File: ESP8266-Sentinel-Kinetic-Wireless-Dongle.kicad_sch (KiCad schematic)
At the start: 55 parts, among them J1 Conn_01x04, J2 Screw_Terminal_01x04, J3 Conn_01x06_Pin, J4 RJ9, J5 Screw_Terminal_01x03, J6 Screw_Terminal_01x02, Q1 AO3400A, SW2 SW_Push, SW4 SW_Push, U1 AMS1117-3.3, U2 ESP-12F, U3 MAX3232, U4 ESP32-WROOM-32, U5 L78L12_SOT89, U6 PC817

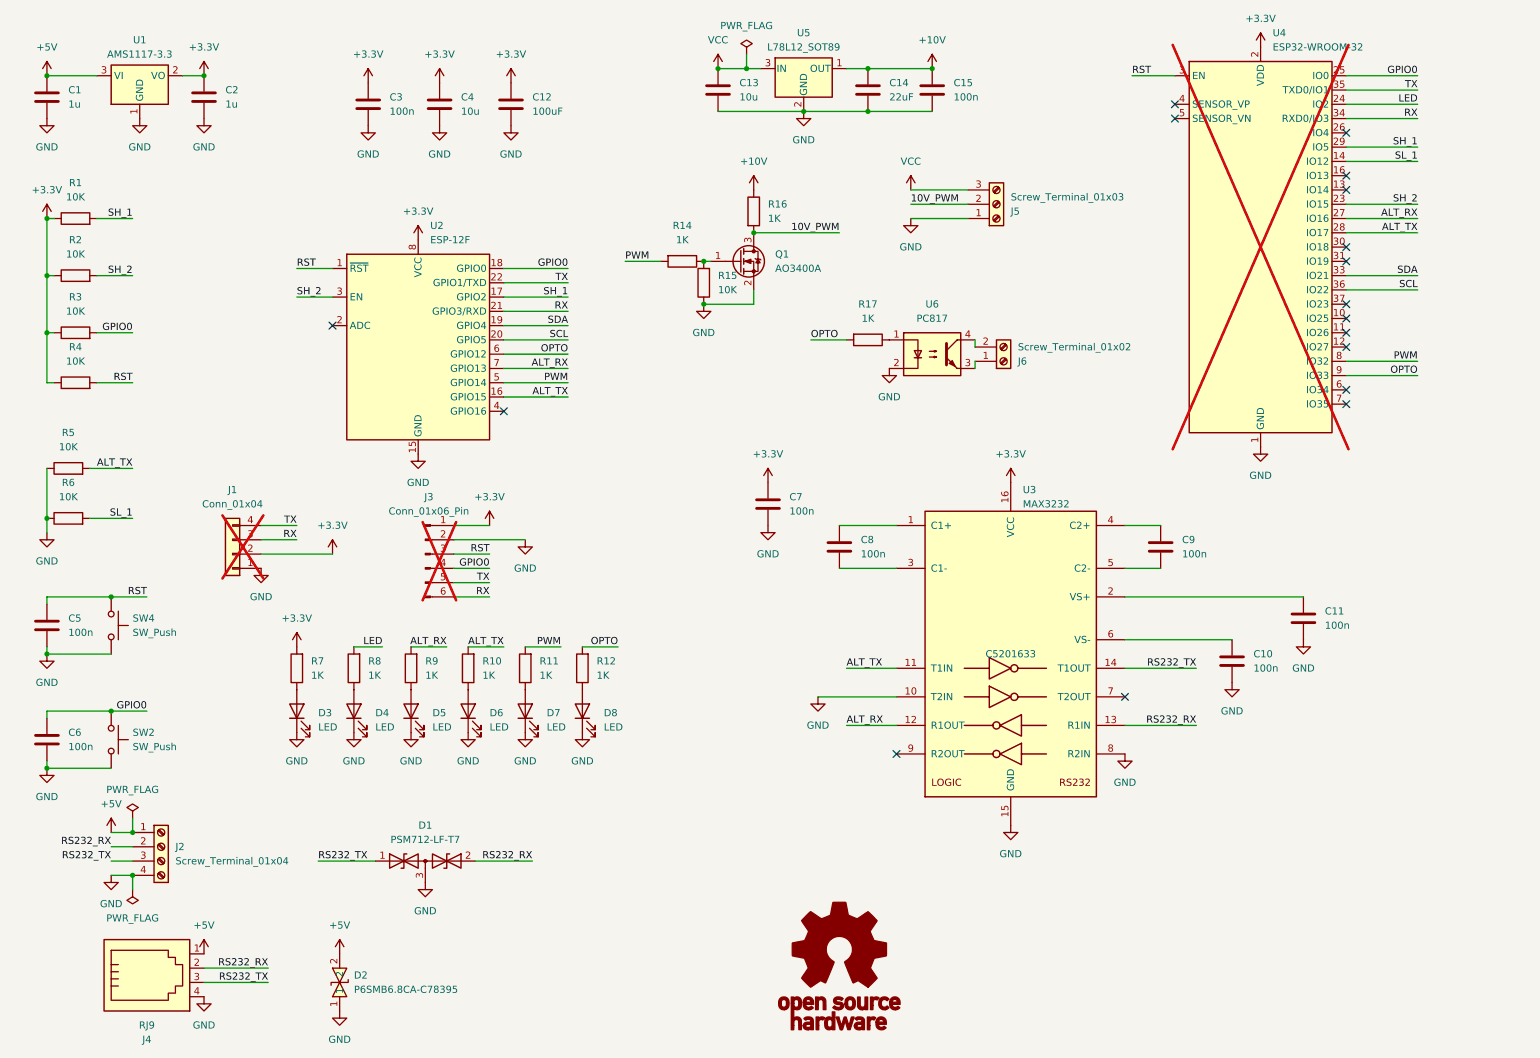
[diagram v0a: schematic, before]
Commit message: Completed PCB Layout Added PWM Rail to rail Added Silkscreen markings
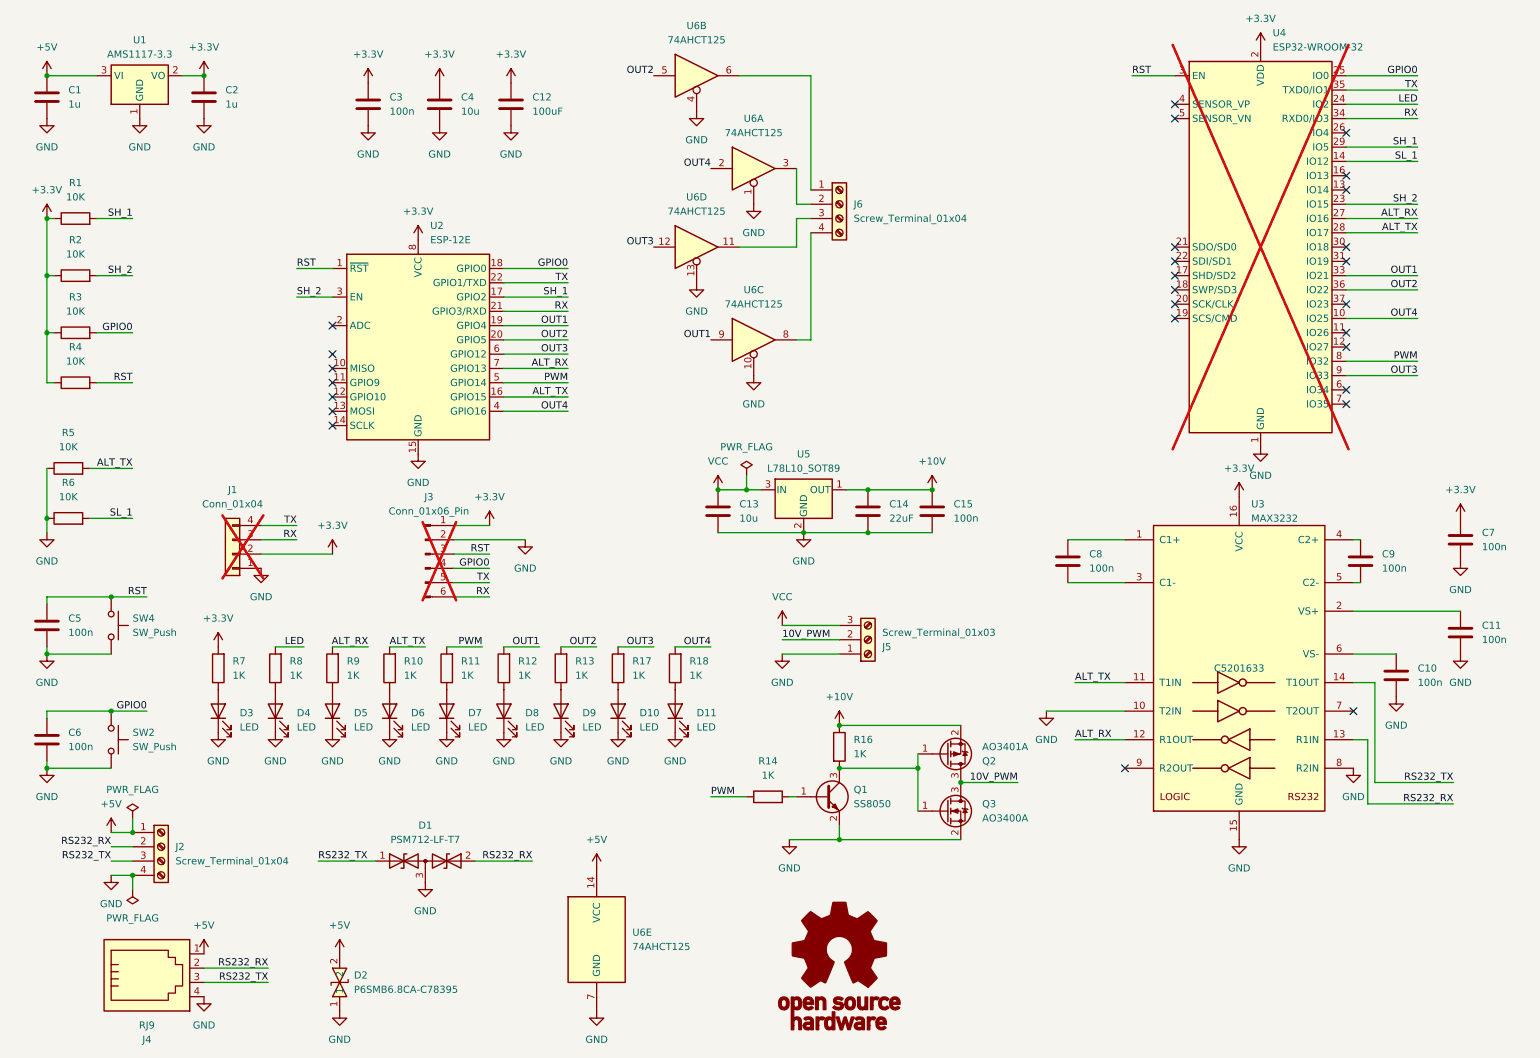
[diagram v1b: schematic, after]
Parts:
- removed J6: Screw_Terminal_01x02, TerminalBlock_4Ucon:TerminalBlock_4Ucon_1x02_P3.50mm_Horizontal, symbol Connector:Screw_Terminal_01x02
- removed Q1: AO3400A, Package_TO_SOT_SMD:SOT-23, symbol Transistor_FET:AO3400A
- removed R15: 10K, Resistor_SMD:R_0402_1005Metric, symbol Device:R
- removed U5: L78L12_SOT89, Package_TO_SOT_SMD:SOT-89-3, symbol Regulator_Linear:L78L12_SOT89
- removed U6: PC817, Package_DIP:DIP-4_W7.62mm, symbol Isolator:PC817
- added D10, D11, D9: LED, LED_SMD:LED_0603_1608Metric, symbol Device:LED
- added J6: Screw_Terminal_01x04, TerminalBlock_4Ucon:TerminalBlock_4Ucon_1x04_P3.50mm_Horizontal, symbol Connector:Screw_Terminal_01x04
- added Q1: SS8050, Package_TO_SOT_SMD:SOT-23, symbol Transistor_BJT:SS8050
- added Q2: AO3401A, Package_TO_SOT_SMD:SOT-23, symbol Transistor_FET:AO3401A
- added Q3: AO3400A, Package_TO_SOT_SMD:SOT-23, symbol Transistor_FET:AO3400A
- added R13, R18: 1K, Resistor_SMD:R_0402_1005Metric, symbol Device:R
- added U5: L78L10_SOT89, Package_TO_SOT_SMD:SOT-89-3, symbol Regulator_Linear:L78L10_SOT89
- added U6: 74AHCT125, Package_DIP:DIP-14_W7.62mm, symbol 74xx:74AHCT125
- U2: value ESP-12F -> ESP-12E
- U4: symbol lib:ESP32-WROOM-32 -> RF_Module:ESP32-WROOM-32
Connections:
- net +10V: now also Q2.2 (S), U5.1 (OUT)
- net +5V: now also U6.14 (VCC)
- net 10V_PWM: now also Q2.3 (D), Q3.3 (D); no longer R16.2
- net GND: now also D10.1 (K), D11.1 (K), D9.1 (K), Q1.2 (E), Q3.2 (S), U5.2 (GND), U6.1, U6.10, U6.13, U6.4, U6.7 (GND)
- net PWM: now also R14.1; no longer R14.2
- net VCC: now also U5.3 (IN)
- net at R17.1: now also D10.2 (A)
- net OUT4: now reaches U4.10 (IO25)
- net OUT4: now also U2.4 (GPIO16), R18.2, U6.2
- net OPTO renamed OUT3
- net OUT3: now also U6.12; no longer R12.2
- net SCL renamed OUT2
- net OUT2: now also R13.2, U6.5
- net SDA renamed OUT1
- net OUT1: now also R12.2, U6.9
- new net: Q1.1 (B), R14.2
- new net: Q1.3 (C), Q2.1 (G), Q3.1 (G), R16.2
- new net: J6.4 (Pin_4), U6.8
- new net: J6.3 (Pin_3), U6.11
- new net: J6.2 (Pin_2), U6.3
- new net: J6.1 (Pin_1), U6.6
- new net: D11.2 (A), R18.1
- new net: D9.2 (A), R13.1
- no-connect marks 17 -> 27
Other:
- moved on the sheet: C10, C11, C13, C14, C15, C7, C8, C9, D3, D4, D5, D6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

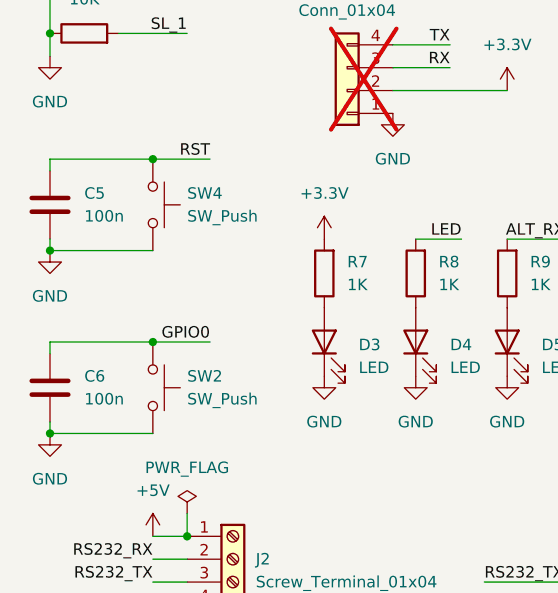
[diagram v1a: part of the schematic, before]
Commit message: Added LCSC Part Numbers
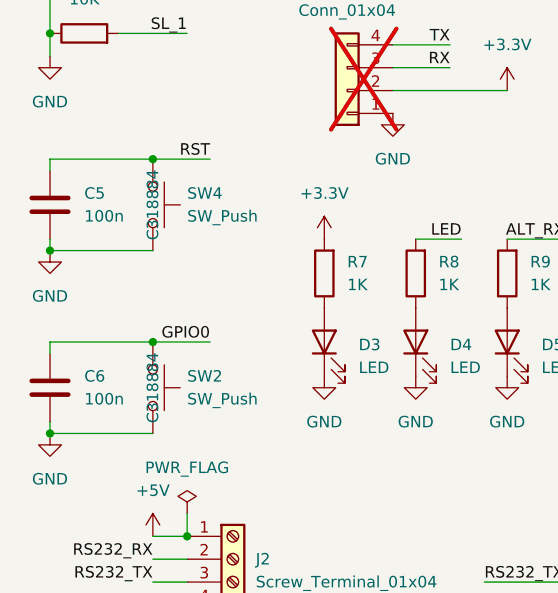
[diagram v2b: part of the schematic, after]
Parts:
- D2: LCSC (none) -> C78395
- SW2, SW4: LCSC (none) -> C318884
- U5: LCSC (none) -> C122848
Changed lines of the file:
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@@
 			)
 		)
+		(property "LCSC" "C122848"
+			(at 154.94 97.79 0)
+			(effects
+				(font
+					(size 1.27 1.27)
+				)
+				(hide yes)
+			)
+		)
 		(pin "3"
 		)
@@
 			)
 		)
-		(property "LCSC" ""
+		(property "LCSC" "C318884"
 			(at 31.75 121.92 0)
 			(effects
@@
 			)
 		)
-		(property "LCSC" ""
+		(property "LCSC" "C318884"
 			(at 31.75 142.24 0)
 			(effects
@@
 			(effects
 				(font
+					(size 1.27 1.27)
+				)
+				(hide yes)
+			)
+		)
+		(property "LCSC" "C78395"
+			(at 72.39 185.42 90)
+			(effects
+				(font
